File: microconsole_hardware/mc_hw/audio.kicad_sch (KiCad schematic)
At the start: 48 parts, among them U5 PCM5102APWR, U6 PAM8302AADCR, U7 PAM8406DR

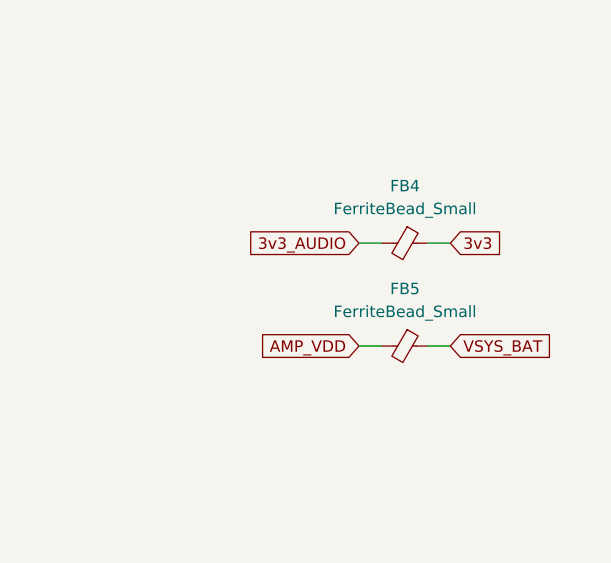
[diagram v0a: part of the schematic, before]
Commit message: fix ferrite beads.
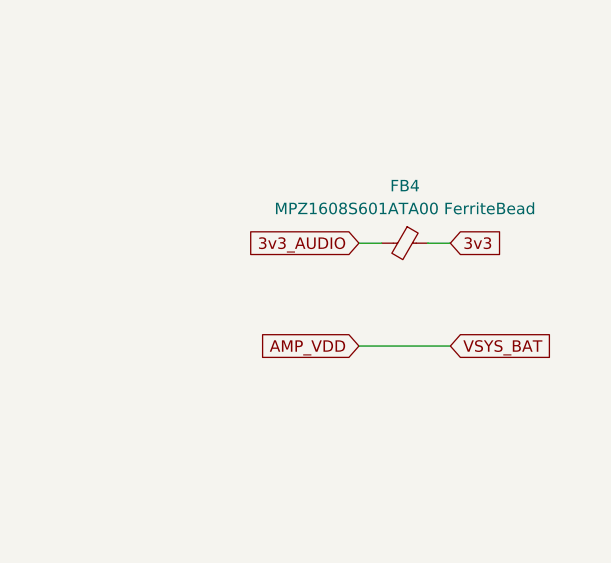
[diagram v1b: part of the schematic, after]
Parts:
- removed FB5: FerriteBead_Small, symbol Device:FerriteBead_Small
- FB4: value FerriteBead_Small -> MPZ1608S601ATA00 FerriteBead; footprint (none) -> Inductor_SMD:L_0603_1608Metric_Pad1.05x0.95mm_HandSolder
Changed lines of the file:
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@@
 	(wire
 		(pts
-			(xy 243.84 55.88) (xy 246.38 55.88)
-		)
-		(stroke
-			(width 0)
-			(type default)
-		)
-	)
-	(wire
-		(pts
 			(xy 185.42 93.98) (xy 185.42 100.33)
 		)
@@
 	(wire
 		(pts
-			(xy 236.22 55.88) (xy 238.76 55.88)
+			(xy 236.22 55.88) (xy 246.38 55.88)
 		)
 		(stroke
@@
 			)
 		)
-		(property "Value" "FerriteBead_Small"
+		(property "Value" "MPZ1608S601ATA00 FerriteBead"
 			(at 241.3381 40.64 90)
 			(show_name no)
@@
 			)
 		)
-		(property "Footprint" ""
+		(property "Footprint" "Inductor_SMD:L_0603_1608Metric_Pad1.05x0.95mm_HandSolder"
 			(at 241.3 42.672 90)
 			(hide yes)
@@
 			)
 		)
-		(property "Datasheet" ""
+		(property "Datasheet" "https://product.tdk.com/system/files/dam/doc/product/emc/emc/beads/catalog/beads_commercial_power_mpz1608_en.pdf"
 			(at 241.3 44.45 0)
 			(hide yes)
@@
 					(unit 1)
 				)
-			)
-		)
-	)
-	(symbol
-		(lib_id "Device:FerriteBead_Small")
-		(at 241.3 55.88 270)
-		(unit 1)
-		(body_style 1)
-		(exclude_from_sim no)
-		(in_bom yes)
-		(on_board yes)
-		(in_pos_files yes)
-		(dnp no)
-		(fields_autoplaced yes)
-		(property "Reference" "FB5"
-			(at 241.3381 49.53 90)
-			(show_name no)
-			(do_not_autoplace no)
-			(effects
-				(font
-					(size 1.27 1.27)
-				)
-			)
-		)
-		(property "Value" "FerriteBead_Small"
-			(at 241.3381 52.07 90)
-			(show_name no)
-			(do_not_autoplace no)
-			(effects
-				(font
-					(size 1.27 1.27)
-				)
-			)
-		)
-		(property "Footprint" ""
-			(at 241.3 54.102 90)
-			(hide yes)
-			(show_name no)
-			(do_not_autoplace no)
-			(effects
-				(font
-					(size 1.27 1.27)
-				)
-			)
-		)
-		(property "Datasheet" ""
-			(at 241.3 55.88 0)
-			(hide yes)
-			(show_name no)
-			(do_not_autoplace no)
-			(effects
-				(font
-					(size 1.27 1.27)
-				)
-			)
-		)
-		(property "Description" "Ferrite bead, small symbol"
-			(at 241.3 55.88 0)
-			(hide yes)
-			(show_name no)
-			(do_not_autoplace no)
-			(effects
-				(font
-					(size 1.27 1.27)
-				)
-			)
-		)
-		(pin "2"
-		)
-		(pin "1"
-		)
-		(instances
-			(project "top"
-				(path "/3433afdc-e53a-48bd-a2b1-9fdee73e8b40/1a1f5339-d8f7-4e0d-9eaf-95ca89a6e02d"
-					(reference "FB5")
-					(unit 1)
-				)
-			)
-			(project "mc_hw"
-				(path "/cf955bee-1207-4d34-b139-374418ecc34e"
-					(reference "FB2")
-					(unit 1)
-				)

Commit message: drc
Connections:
- net AMP_VDD renamed VSYS_BAT
- net VSYS_BAT: no longer C43.2, U7.13 (PVDDR)
- new net: C43.2, U7.13 (PVDDR)
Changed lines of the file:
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@@
 	(wire
 		(pts
-			(xy 177.8 102.87) (xy 185.42 102.87)
+			(xy 177.8 102.87) (xy 207.01 102.87)
 		)
 		(stroke
@@
 	(wire
 		(pts
-			(xy 236.22 55.88) (xy 246.38 55.88)
-		)
-		(stroke
-			(width 0)
-			(type default)
-		)
-	)
-	(wire
-		(pts
 			(xy 190.5 116.84) (xy 190.5 118.11)
 		)
@@
 	(wire
 		(pts
-			(xy 185.42 93.98) (xy 195.58 93.98)
+			(xy 185.42 93.98) (xy 205.74 93.98)
 		)
 		(stroke
@@
 		)
 	)
-	(global_label "AMP_VDD"
+	(global_label "VSYS_BAT"
 		(shape input)
 		(at 76.2 105.41 180)
@@
 		)
 		(property "Intersheetrefs" "${INTERSHEET_REFS}"
-			(at 64.8086 105.41 0)
+			(at 64.3248 105.41 0)
 			(hide yes)
 			(show_name no)
@@
 		)
 	)
+	(global_label "VSYS_BAT"
+		(shape input)
+		(at 99.06 102.87 180)
+		(fields_autoplaced yes)
+		(effects
+			(font
+				(size 1.27 1.27)
+			)
+			(justify right)
+		)
+		(property "Intersheetrefs" "${INTERSHEET_REFS}"
+			(at 87.1848 102.87 0)
+			(hide yes)
+			(show_name no)
+			(do_not_autoplace no)
+			(effects
+				(font
+					(size 1.27 1.27)
+				)
+				(justify right)
+			)
+		)
+	)
 	(global_label "GND"
 		(shape input)
@@
 		)
 	)
-	(global_label "AMP_VDD"
+	(global_label "VSYS_BAT"
 		(shape input)
 		(at 166.37 110.49 0)
@@
 		)
 		(property "Intersheetrefs" "${INTERSHEET_REFS}"
-			(at 177.7614 110.49 0)
+			(at 178.2452 110.49 0)
 			(hide yes)
 			(show_name no)
@@
 		)
 	)
-	(global_label "AMP_VDD"
-		(shape input)
-		(at 195.58 93.98 0)
-		(fields_autoplaced yes)
-		(effects
-			(font
-				(size 1.27 1.27)
-			)
-			(justify left)
-		)
-		(property "Intersheetrefs" "${INTERSHEET_REFS}"
-			(at 206.9714 93.98 0)
-			(hide yes)
-			(show_name no)
-			(do_not_autoplace no)
-			(effects
-				(font
-					(size 1.27 1.27)
-				)
-				(justify left)
-			)
-		)
-	)
-	(global_label "AMP_VDD"
+	(global_label "VSYS_BAT"
 		(shape input)
 		(at 97.79 160.02 180)
@@
 		)
 		(property "Intersheetrefs" "${INTERSHEET_REFS}"
-			(at 86.3986 160.02 0)
+			(at 85.9148 160.02 0)
 			(hide yes)
 			(show_name no)
@@
 		)
 	)
-	(global_label "AMP_VDD"
+	(global_label "VSYS_BAT"
 		(shape input)
-		(at 185.42 102.87 0)
+		(at 207.01 102.87 0)
 		(fields_autoplaced yes)
 		(effects
@@
 		)
 		(property "Intersheetrefs" "${INTERSHEET_REFS}"
-			(at 196.8114 102.87 0)
+			(at 218.8852 102.87 0)
 			(hide yes)
 			(show_name no)
@@
 		)
 	)
-	(global_label "AMP_VDD"
+	(global_label "VSYS_BAT"
 		(shape input)
 		(at 101.6 92.71 180)
@@
 		)
 		(property "Intersheetrefs" "${INTERSHEET_REFS}"
-			(at 90.2086 92.71 0)
+			(at 89.7248 92.71 0)
 			(hide yes)
 			(show_name no)
@@
 		)
 	)
-	(global_label "AMP_VDD"
-		(shape input)
-		(at 99.06 102.87 180)
-		(fields_autoplaced yes)
-		(effects
-			(font
-				(size 1.27 1.27)
-			)
-			(justify right)
-		)
-		(property "Intersheetrefs" "${INTERSHEET_REFS}"
-			(at 87.6686 102.87 0)
-			(hide yes)
-			(show_name no)
-			(do_not_autoplace no)
-			(effects
-				(font
-					(size 1.27 1.27)
-				)
-				(justify right)
-			)
-		)
-	)
 	(global_label "GPIO20 {slash} MAX DIN"
 		(shape input)
@@
 		)
 	)
-	(global_label "VSYS_BAT"
-		(shape input)
-		(at 246.38 55.88 0)
-		(fields_autoplaced yes)
-		(effects
-			(font
-				(size 1.27 1.27)
-			)
-			(justify left)
-		)
-		(property "Intersheetrefs" "${INTERSHEET_REFS}"
-			(at 258.2552 55.88 0)
-			(hide yes)
-			(show_name no)
-			(do_not_autoplace no)
-			(effects
-				(font
-					(size 1.27 1.27)
-				)
-				(justify left)
-			)
-		)
-	)
 	(global_label "VOL_ADC"
 		(shape input)
@@
 		)
 	)
-	(global_label "AMP_VDD"
+	(global_label "VSYS_BAT"
 		(shape input)
 		(at 152.4 175.26 0)
@@
 		)
 		(property "Intersheetrefs" "${INTERSHEET_REFS}"
-			(at 163.7914 175.26 0)
+			(at 164.2752 175.26 0)
 			(hide yes)
 			(show_name no)
@@
 		)
 	)
-	(global_label "AMP_VDD"
-		(shape input)
-		(at 236.22 55.88 180)
-		(fields_autoplaced yes)
-		(effects
-			(font
-				(size 1.27 1.27)
-			)
-			(justify right)
-		)
-		(property "Intersheetrefs" "${INTERSHEET_REFS}"
-			(at 224.8286 55.88 0)
-			(hide yes)
-			(show_name no)
-			(do_not_autoplace no)
-			(effects
-				(font
-					(size 1.27 1.27)
-				)
-				(justify right)
-			)
-		)
-	)
 	(global_label "GND"
 		(shape input)
@@
 		)
 		(property "Voltage" "25V"
-			(at 90.17 182.88 0)
+			(at 99.06 184.15 90)
 			(show_name no)
 			(do_not_autoplace no)
@@
 		)
 		(property "Tolerance" "20%"
-			(at 87.63 182.88 0)
+			(at 99.06 186.69 90)
 			(show_name no)
 			(do_not_autoplace no)

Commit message: fixup things
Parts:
- R18, R19: value 470 OHM -> 470
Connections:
- net VSYS_BAT: now also C43.2, U7.13 (PVDDR)
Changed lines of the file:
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@@
 		)
 	)
+	(global_label "VSYS_BAT"
+		(shape input)
+		(at 205.74 93.98 0)
+		(fields_autoplaced yes)
+		(effects
+			(font
+				(size 1.27 1.27)
+			)
+			(justify left)
+		)
+		(property "Intersheetrefs" "${INTERSHEET_REFS}"
+			(at 217.6152 93.98 0)
+			(hide yes)
+			(show_name no)
+			(do_not_autoplace no)
+			(effects
+				(font
+					(size 1.27 1.27)
+				)
+				(justify left)
+			)
+		)
+	)
 	(global_label "3v3"
 		(shape input)
@@
 			)
 		)
-		(property "Value" "470 OHM"
+		(property "Value" "470"
 			(at 64.77 43.942 0)
 			(show_name no)
@@
 		)
 		(property "Voltage" "25V"
-			(at 52.07 54.61 0)
+			(at 56.642 52.07 0)
 			(show_name no)
 			(do_not_autoplace no)
@@
 		)
 		(property "Tolerance" "20%"
-			(at 52.07 57.15 0)
+			(at 56.642 54.61 0)
 			(show_name no)
 			(do_not_autoplace no)
@@
 		)
 		(property "Voltage" "25V"
-			(at 52.07 64.77 0)
+			(at 56.388 62.23 0)
 			(show_name no)
 			(do_not_autoplace no)
@@
 		)
 		(property "Tolerance" "20%"
-			(at 52.07 67.31 0)
+			(at 56.388 64.77 0)
 			(show_name no)
 			(do_not_autoplace no)
@@
 			)
 		)
-		(property "Value" "470 OHM"
+		(property "Value" "470"
 			(at 64.77 54.102 0)
 			(show_name no)
@@
 		(dnp no)
 		(property "Reference" "C22"
-			(at 63.754 35.814 90)
+			(at 62.738 35.306 90)
 			(show_name no)
 			(do_not_autoplace no)
@@
 		)
 		(property "Voltage" "25V"
-			(at 60.96 34.29 0)
+			(at 70.104 35.56 90)
 			(show_name no)
 			(do_not_autoplace no)
@@
 		)
 		(property "Tolerance" "20%"
-			(at 58.42 34.29 0)
+			(at 70.104 38.1 90)
 			(show_name no)
 			(do_not_autoplace no)

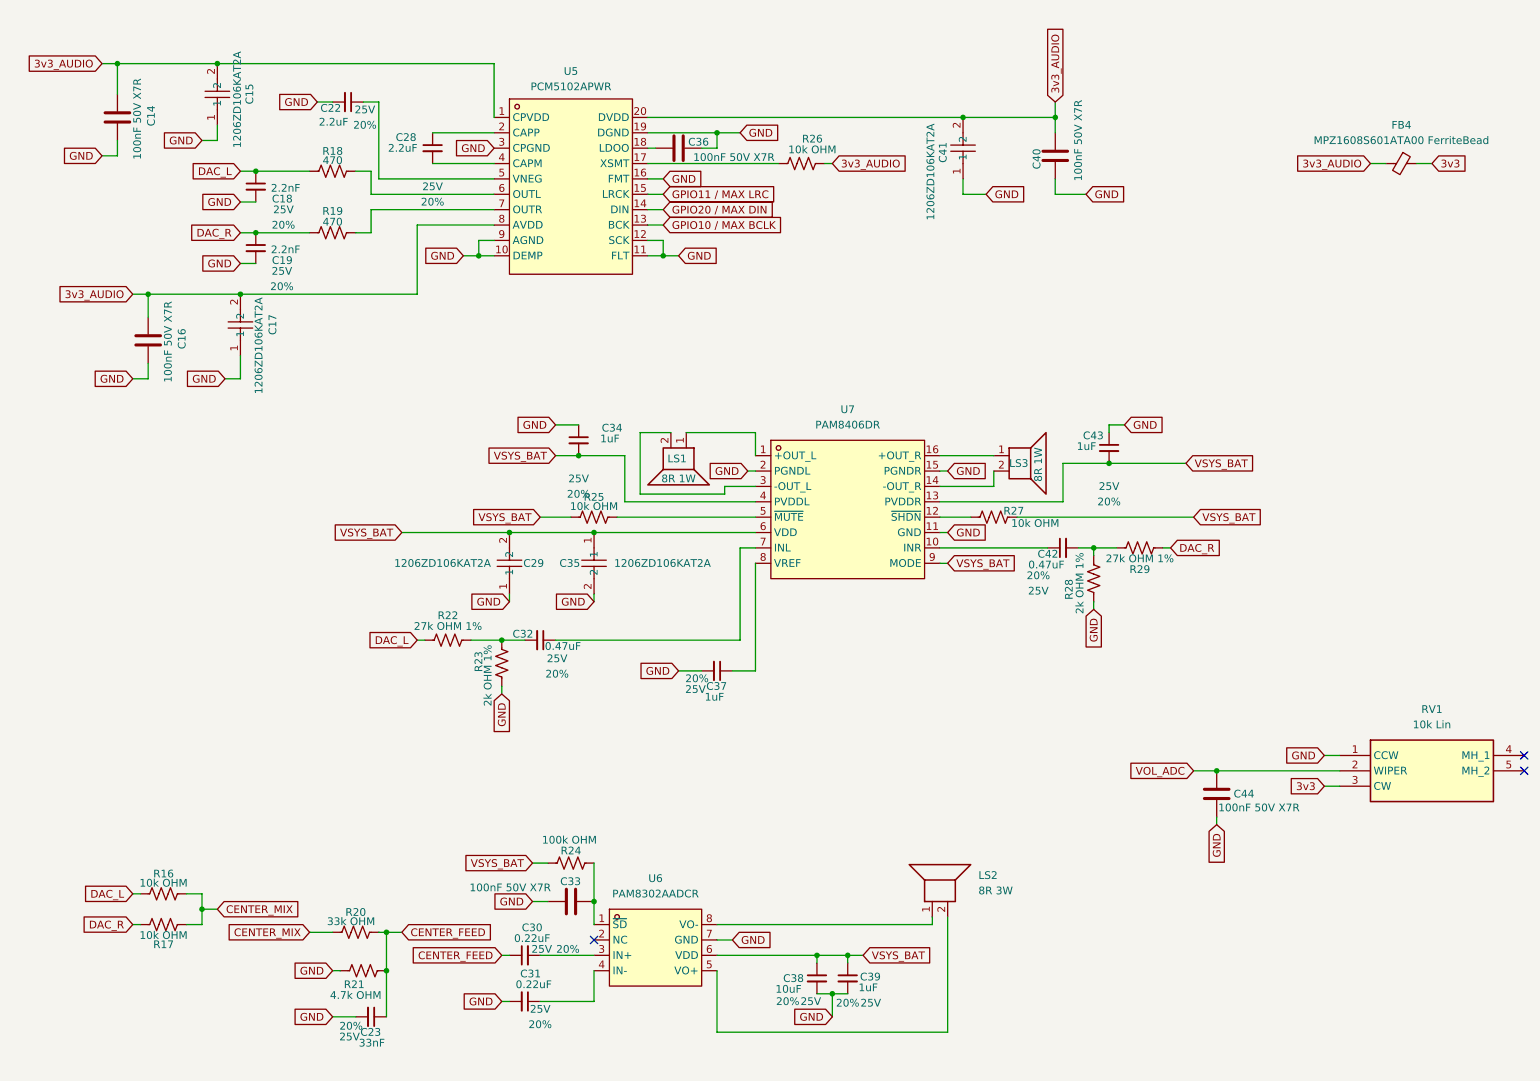
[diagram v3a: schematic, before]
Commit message: resistor and capacitor consolidation.
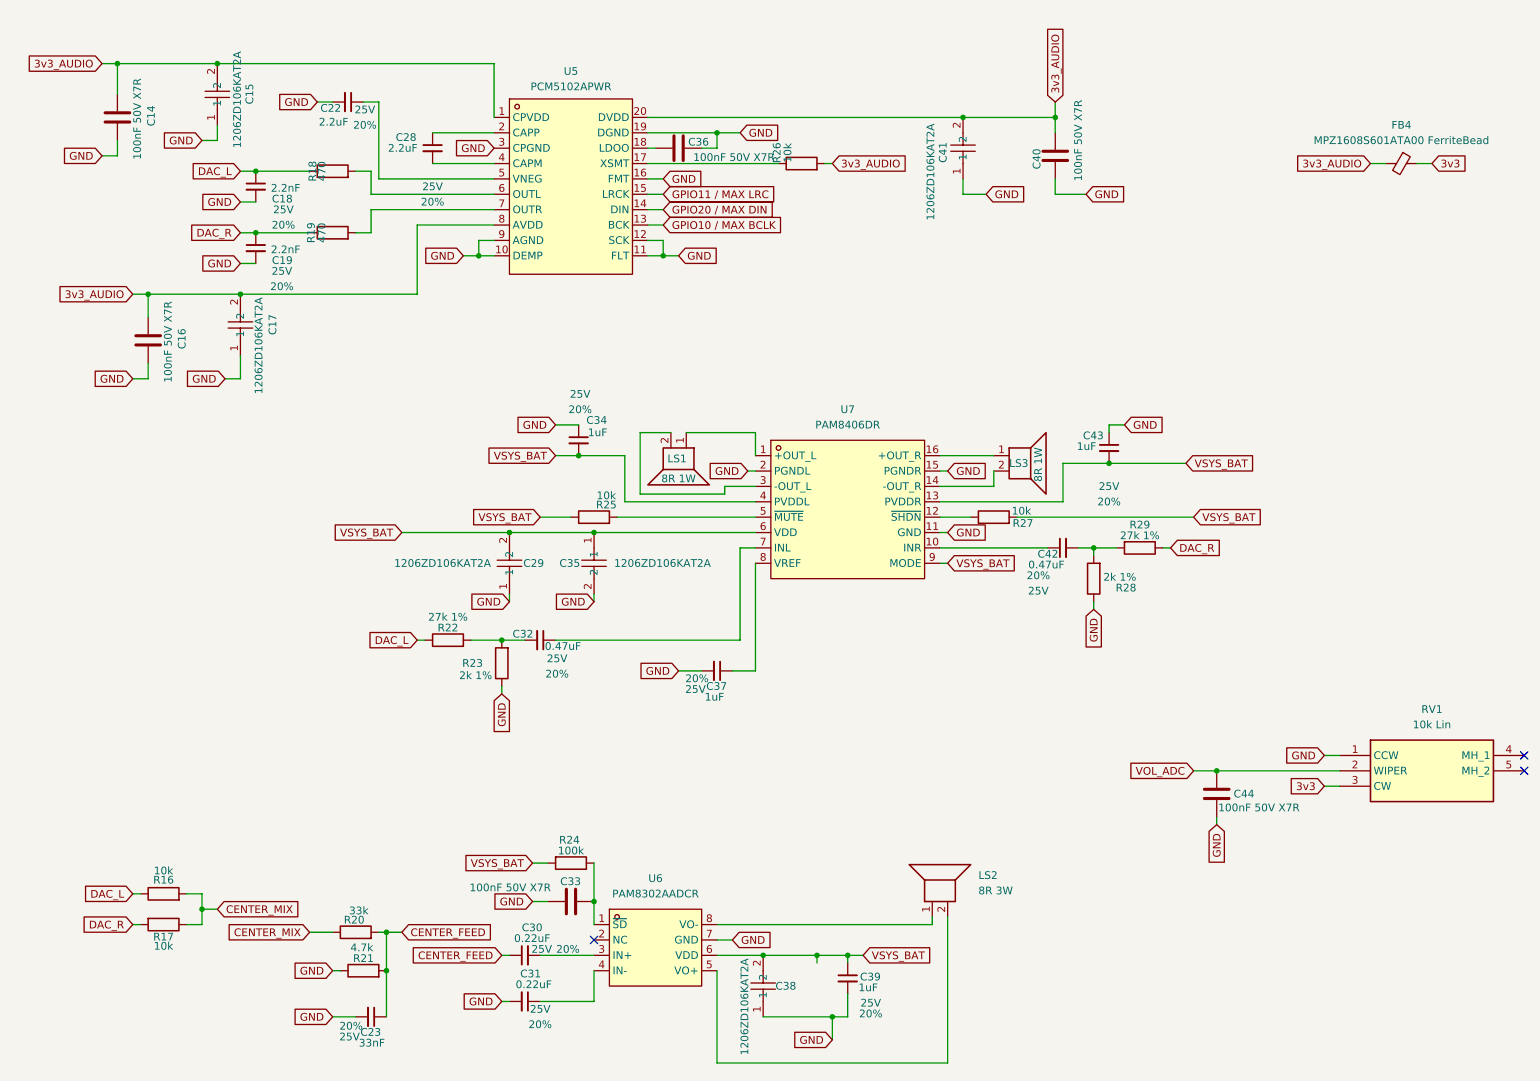
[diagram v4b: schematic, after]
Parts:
- removed C38: 10uF, PCM_SparkFun-Capacitor:C_0805_2012Metric, symbol PCM_SparkFun-Capacitor:2.2uF_0805_25V_20%
- added C38: 1206ZD106KAT2A, project_parts:C1206, symbol project_parts:1206ZD106KAT2A
- R16, R17, R25, R26, R27: value 10k OHM -> 10k; footprint PCM_SparkFun-Resistor:R_0603_1608Metric -> Resistor_SMD:R_0603_1608Metric; symbol PCM_SparkFun-Resistor:R -> Device:R
- R18, R19: footprint PCM_SparkFun-Resistor:R_0603_1608Metric -> Resistor_SMD:R_0603_1608Metric; symbol PCM_SparkFun-Resistor:R -> Device:R
- R20: value 33k OHM -> 33k; footprint PCM_SparkFun-Resistor:R_0603_1608Metric -> Resistor_SMD:R_0603_1608Metric; symbol PCM_SparkFun-Resistor:R -> Device:R
- R21: value 4.7k OHM -> 4.7k; footprint PCM_SparkFun-Resistor:R_0603_1608Metric -> Resistor_SMD:R_0603_1608Metric; symbol PCM_SparkFun-Resistor:R -> Device:R
- R22, R29: value 27k OHM 1% -> 27k 1%; footprint PCM_SparkFun-Resistor:R_0603_1608Metric -> Resistor_SMD:R_0603_1608Metric; symbol PCM_SparkFun-Resistor:R -> Device:R
- R23, R28: value 2k OHM 1% -> 2k 1%; footprint PCM_SparkFun-Resistor:R_0603_1608Metric -> Resistor_SMD:R_0603_1608Metric; symbol PCM_SparkFun-Resistor:R -> Device:R
- R24: value 100k OHM -> 100k; footprint PCM_SparkFun-Resistor:R_0603_1608Metric -> Resistor_SMD:R_0603_1608Metric; symbol PCM_SparkFun-Resistor:R -> Device:R
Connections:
- net 3v3_AUDIO: now also R26.2; no longer R26.1
- net CENTER_FEED: now also R20.2, R21.2; no longer R20.1, R21.1
- net CENTER_MIX: now also R16.2, R17.1, R20.1; no longer R16.1, R17.2, R20.2
- net DAC_L: now also R16.1, R18.1, R22.1; no longer R16.2, R18.2, R22.2
- net DAC_R: now also R17.2, R19.1, R29.1; no longer R17.1, R19.2, R29.2
- net GND: now also R21.1, R23.1, R28.1, C38.1; no longer R21.2, R23.2, R28.2
- net VSYS_BAT: now also R24.2, R25.1, R27.2, C38.2; no longer R24.1, R25.2, R27.1
- net at U5.6 (OUTL): now also R18.2; no longer R18.1
- net at C33.2, U6.1 (~{SD}): now also R24.1; no longer R24.2
- net at U7.12 (~{SHDN}): now also R27.1; no longer R27.2
- net at U7.5 (~{MUTE}): now also R25.2; no longer R25.1
- net at U5.17 (XSMT): now also R26.1; no longer R26.2
- net at U5.7 (OUTR): now also R19.2; no longer R19.1
- new net: C42.2, R28.2, R29.2
- new net: C32.2, R22.2, R23.2
